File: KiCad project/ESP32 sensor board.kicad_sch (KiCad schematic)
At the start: 25 parts, among them J1 USB_C_Receptacle, J2 JST_2mm_LiPo, U1 MCP73871, U2 LM1117MPX-3.3_NOPB

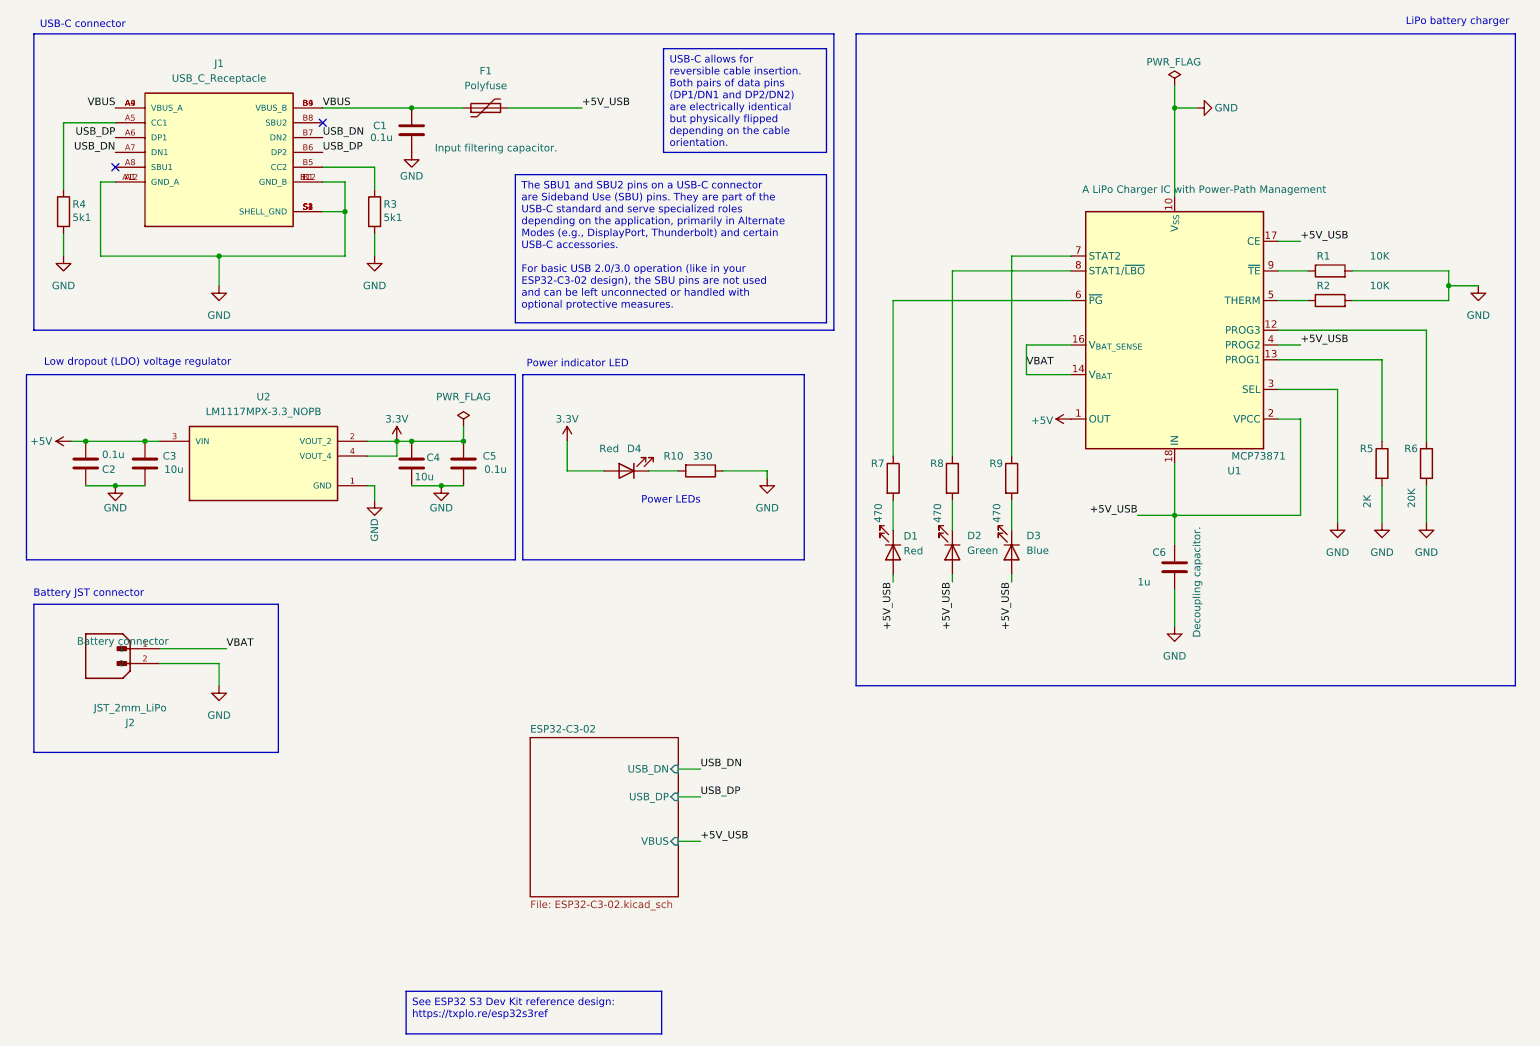
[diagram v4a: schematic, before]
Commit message: Replaced tantalum capacitors and LEDs.
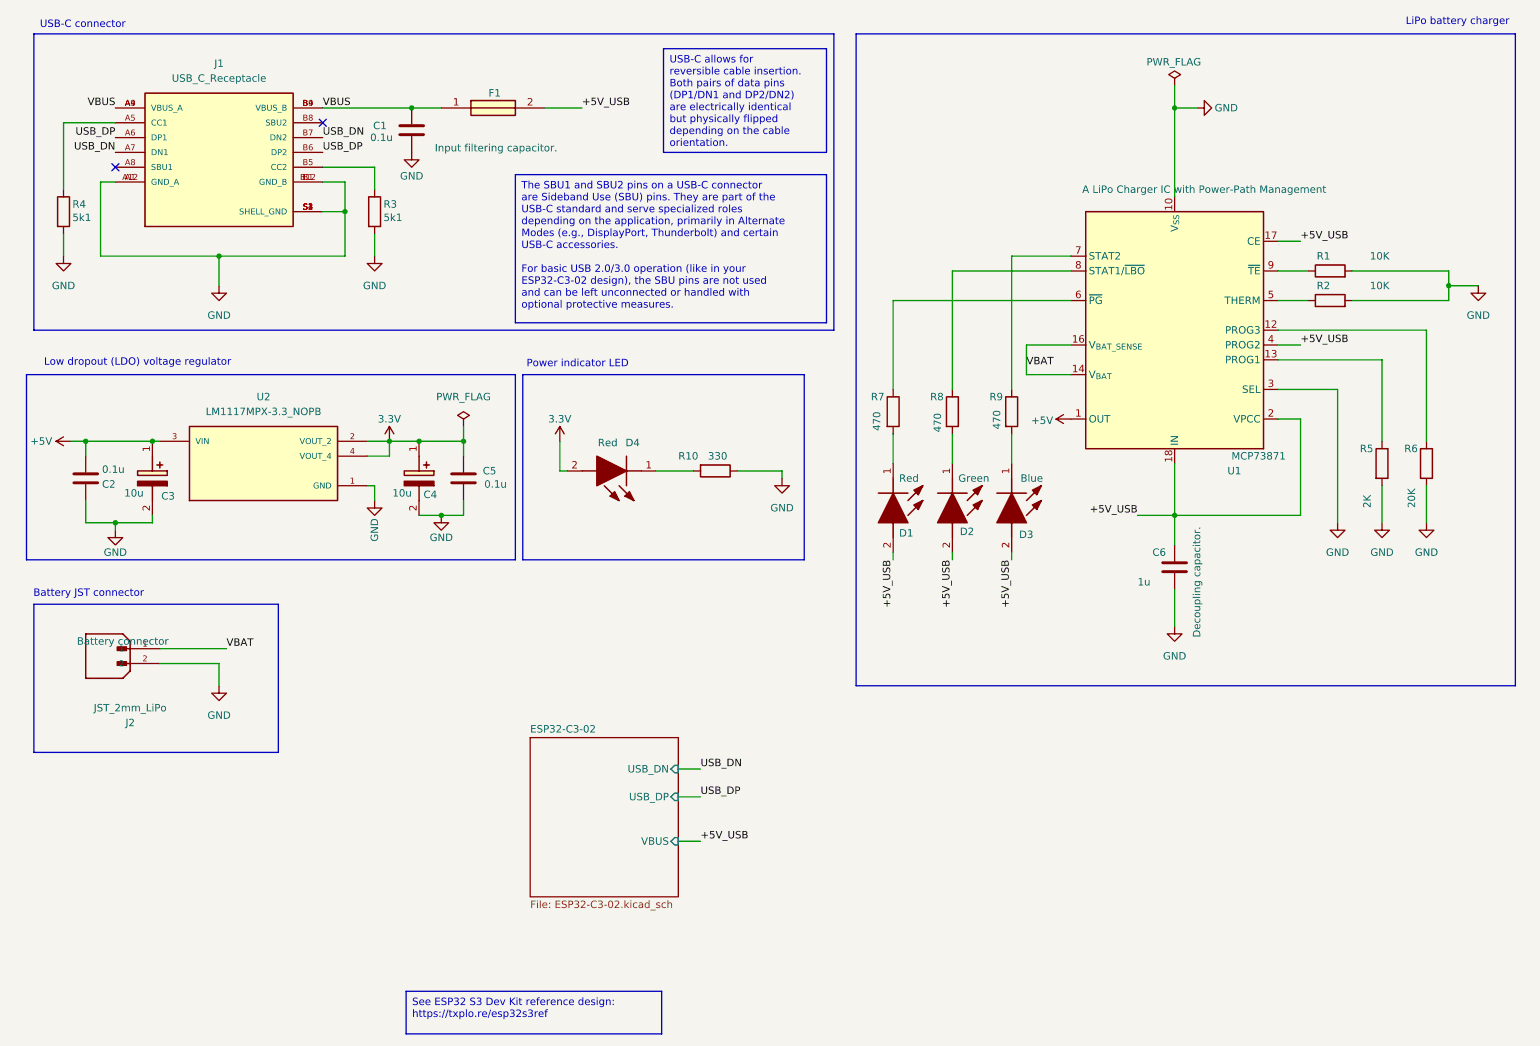
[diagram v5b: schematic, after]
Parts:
- removed F1: Polyfuse, Fuse:Fuse_1210_3225Metric, symbol SparkFun-Fuse:Fuse 6V/2.0A/4.0A
- added F1: 0ZCH0110AF2E, Footprints:FUSC3226X100N, symbol SamacSys_Parts:0ZCH0110AF2E
- C3: footprint Capacitor_SMD:C_0805_2012Metric -> T491A; symbol SparkFun-Capacitor:C -> T491A106K010AT7280:T491A106K010AT7280; Arrow Part Number (none) -> T491A106K010AT7280; Arrow Price/Stock (none) -> https://www.arrow.com/en/products/t491a106k010at7280/kemet-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; Comments (none) -> Download this part from https://componentsearchengine.com/p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; Height (none) -> 1.8; Manufacturer_Name (none) -> KEMET; Manufacturer_Part_Number (none) -> T491A106K010AT7280; Mouser Part Number (none) -> 80-T491A106K107280; Mouser Price/Stock (none) -> https://www.mouser.co.uk/ProductDetail/KEMET/T491A106K010AT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
- C4: footprint Capacitor_SMD:C_0805_2012Metric -> T491A; symbol SparkFun-Capacitor:C -> T491A106K010AT7280:T491A106K010AT7280; Arrow Part Number (none) -> T491A106K010AT7280; Arrow Price/Stock (none) -> https://www.arrow.com/en/products/t491a106k010at7280/kemet-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; Height (none) -> 1.8; Manufacturer_Name (none) -> KEMET; Manufacturer_Part_Number (none) -> T491A106K010AT7280; Mouser Part Number (none) -> 80-T491A106K107280; Mouser Price/Stock (none) -> https://www.mouser.co.uk/ProductDetail/KEMET/T491A106K010AT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
- D1: footprint LED_SMD:LED_0603_1608Metric -> LEDC2012X120N; symbol SparkFun-LED:LED_Red_0603 -> LTST-C170KRKT:LTST-C170KRKT; Arrow Part Number (none) -> LTST-C170KRKT; Arrow Price/Stock (none) -> https://www.arrow.com/en/products/ltst-c170krkt/lite-on-tec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; Height (none) -> 1.2; Manufacturer_Name (none) -> Lite-On; Manufacturer_Part_Number (none) -> LTST-C170KRKT; Mouser Part Number (none) -> 859-LTST-C170KRKT; Mouser Price/Stock (none) -> https://www.mouser.co.uk/ProductDetail/Lite-On/LTST-C170KRK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
- D2: footprint LED_SMD:LED_0603_1608Metric -> LEDC2012X120N; symbol SparkFun-LED:LED_Green_0603 -> LTST-C170GKT:LTST-C170GKT; Arrow Part Number (none) -> LTST-C170GKT; Arrow Price/Stock (none) -> https://www.arrow.com/en/products/ltst-c170gkt/lite-on-tech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; Comments (none) -> Download part from https://componentsearchengine.com/part-v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; Height (none) -> 1.2; Manufacturer_Name (none) -> Lite-On; Manufacturer_Part_Number (none) -> LTST-C170GKT; Mouser Part Number (none) -> 859-LTST-C170GKT; Mouser Price/Stock (none) -> https://www.mouser.co.uk/ProductDetail/Lite-On/LTST-C170GKT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
- D3: footprint LED_SMD:LED_0603_1608Metric -> LEDC2012X120N; symbol SparkFun-LED:LED_Blue_0603 -> LTST-C170TBKT:LTST-C170TBKT; Arrow Part Number (none) -> LTST-C170TBKT; Arrow Price/Stock (none) -> https://www.arrow.com/en/products/ltst-c170tbkt/lite-on-tec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; Comments (none) -> Download from https://componentsearchengine.com/part-view/L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; Height (none) -> 1.2; Manufacturer_Name (none) -> Lite-On; Manufacturer_Part_Number (none) -> LTST-C170TBKT; Mouser Part Number (none) -> 859-LTST-C170TBKT; Mouser Price/Stock (none) -> https://www.mouser.co.uk/ProductDetail/Lite-On/LTST-C170TBK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
- D4: footprint LED_SMD:LED_0603_1608Metric -> LEDC2012X120N; symbol SparkFun-LED:LED_Red_0603 -> LTST-C170KRKT:LTST-C170KRKT; Arrow Part Number (none) -> LTST-C170KRKT; Arrow Price/Stock (none) -> https://www.arrow.com/en/products/ltst-c170krkt/lite-on-tec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; Comments (none) -> Download from https://componentsearchengine.com/part-view/L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; Height (none) -> 1.2; Manufacturer_Name (none) -> Lite-On; Manufacturer_Part_Number (none) -> LTST-C170KRKT; Mouser Part Number (none) -> 859-LTST-C170KRKT; Mouser Price/Stock (none) -> https://www.mouser.co.uk/ProductDetail/Lite-On/LTST-C170KRK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
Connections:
- net +5V_USB: now also F1.2
- net VBUS: now also F1.1
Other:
- note removed: "Power LEDs"
- moved on the sheet: C2, C5, R10, R7, R8, R9

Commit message: Completed draft of the layout.
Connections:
- net CHARGING_POWER_GOOD: now reaches R7.1, U1.6 (~{PG})
- net PWR_LED: now reaches D4.1 (K), R10.2
- net CHARGED: now reaches R8.1, U1.8 (STAT1/~{LBO})
- net CHARGING: now reaches R9.1, U1.7 (STAT2)
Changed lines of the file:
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@@
+		)
+	)
+	(label "CHARGING_POWER_GOOD"
+		(at 172.72 63.5 90)
+		(fields_autoplaced yes)
+		(effects
+			(font
+				(size 1.27 1.27)
+			)
+			(justify left bottom)
 		)
 	)
@@
 		)
 	)
+	(label "PWR_LED"
+		(at 132.08 92.71 90)
+		(fields_autoplaced yes)
+		(effects
+			(font
+				(size 1.27 1.27)
+			)
+			(justify left bottom)
+		)
+	)
 	(label "USB_DP"
 		(at 36.83 35.56 180)
@@
 		)
 	)
+	(label "CHARGING"
+		(at 194.31 55.88 90)
+		(fields_autoplaced yes)
+		(effects
+			(font
+				(size 1.27 1.27)
+			)
+			(justify left bottom)
+		)
+	)
 	(label "+5V_USB"
 		(at 240.03 71.12 0)
 		(fields_autoplaced yes)
 		(effects
+			(font
+				(size 1.27 1.27)
+			)
+			(justify left bottom)
+		)
+	)
+	(label "CHARGED"
+		(at 182.88 58.42 90)
+		(fields_autoplaced yes)
+		(effects

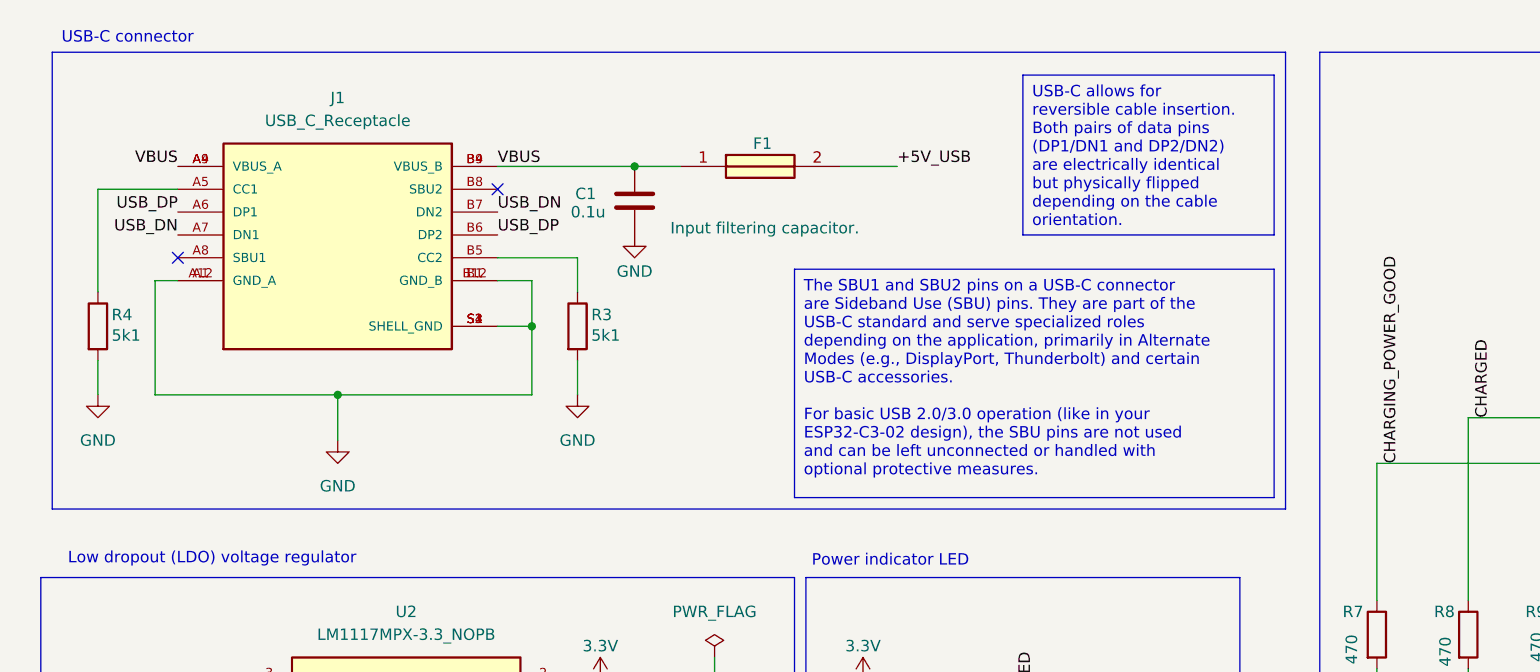
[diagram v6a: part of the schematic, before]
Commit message: Replaced USB C receptacle with a different model. Repositioning components to better align with manufacturer recommendations.
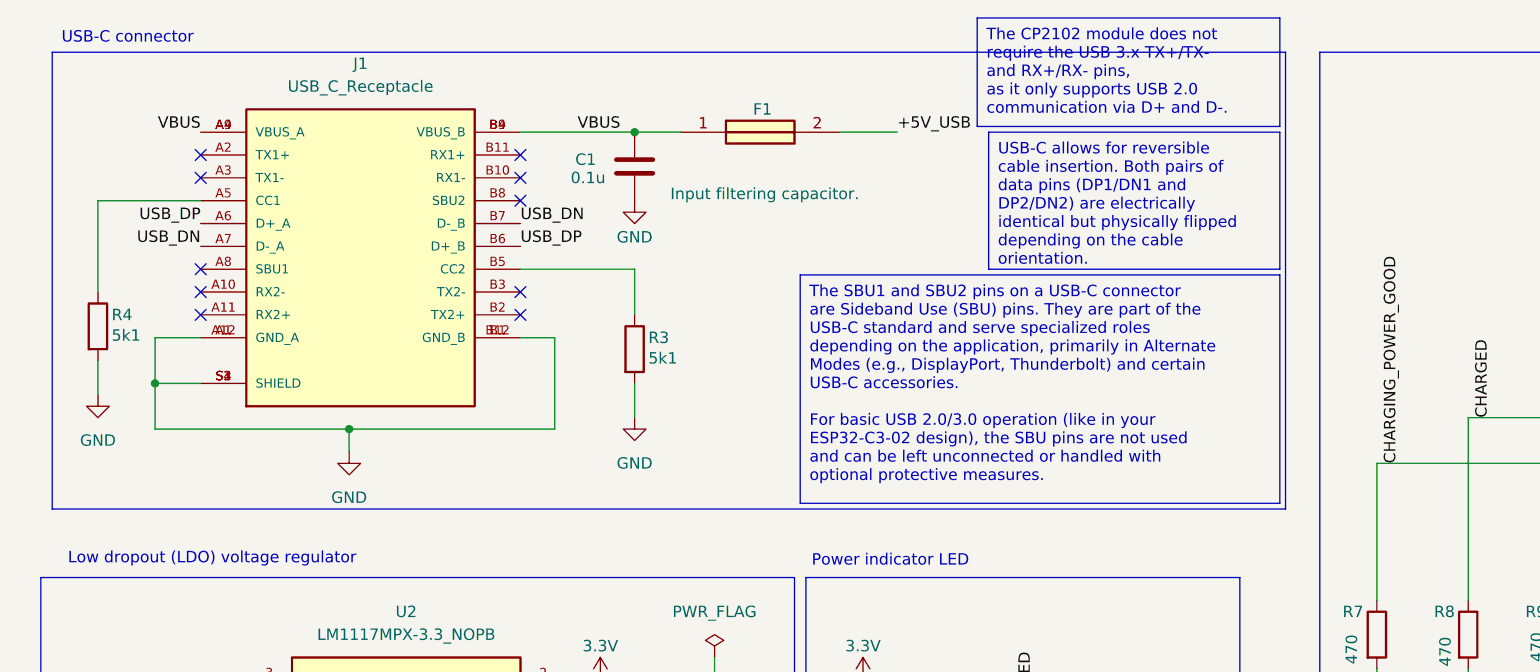
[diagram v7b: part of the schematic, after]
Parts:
- J1: footprint Footprints:VALCON_CSP-USC16-TR -> Footprints:TE_1-2295018-2; symbol CSP-USC16-TR:CSP-USC16-TR -> 1-2295018-2:1-2295018-2; Check_prices https://www.snapeda.com/parts/CSP-USC16-TR/Valcon/view-part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 -> https://www.snapeda.com/parts/1-2295018-2/TE+Connectivity/v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; Comment (none) -> 1-2295018-2; Description_1 CSP-USC16-TR Valcon USB Type C Surface Mount PCB Socket -> USB TYPE C, REC OFFSET 0.65MM DUAL SMT; MANUFACTURER Valcon -> TE Connectivity; MAXIMUM_PACKAGE_HEIGHT 3.26 mm -> 3.6 mm; MF Valcon -> TE Connectivity; MP CSP-USC16-TR -> 1-2295018-2; PARTREV A0 -> B1; SnapEDA_Link https://www.snapeda.com/parts/CSP-USC16-TR/Valcon/view-part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 -> https://www.snapeda.com/parts/1-2295018-2/TE+Connectivity/v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
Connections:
- no-connect marks 2 -> 10
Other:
- moved on the sheet: C1, F1, R3

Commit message: Work in progress, new layout and routing.
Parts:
- C3, C4: footprint T491A -> Footprints:T491A
- D1, D2, D3, D4: footprint LEDC2012X120N -> Footprints:LEDC2012X120N
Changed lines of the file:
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@@
 			)
 		)
-		(property "Footprint" "T491A"
+		(property "Footprint" "Footprints:T491A"
 			(at -7.29 96.52 0)
 			(effects
@@
 			)
 		)
-		(property "Footprint" "LEDC2012X120N"
+		(property "Footprint" "Footprints:LEDC2012X120N"
 			(at 116.84 -0.94 0)
 			(effects
@@
 			)
 		)
-		(property "Footprint" "T491A"
+		(property "Footprint" "Footprints:T491A"
 			(at -53.01 96.52 0)
 			(effects
@@
 			)
 		)
-		(property "Footprint" "LEDC2012X120N"
+		(property "Footprint" "Footprints:LEDC2012X120N"
 			(at 76.53 104.14 0)
 			(effects
@@
 			)
 		)
-		(property "Footprint" "LEDC2012X120N"
+		(property "Footprint" "Footprints:LEDC2012X120N"
 			(at 86.69 104.14 0)
 			(effects
@@
 			)
 		)
-		(property "Footprint" "LEDC2012X120N"
+		(property "Footprint" "Footprints:LEDC2012X120N"
 			(at 96.85 104.14 0)
 			(effects
